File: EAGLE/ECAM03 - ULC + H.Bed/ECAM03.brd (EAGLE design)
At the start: 160 x 60 mm, 45 parts, among them J1 MODULAR TOOL, J2 FAN1, J3 FAN2, J4 FAN3, J5 B4B-PH-SM4, J6 SSR, J7 RINGLIGHT, J8 FTDI, J9 SPI, Q2 16MHz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

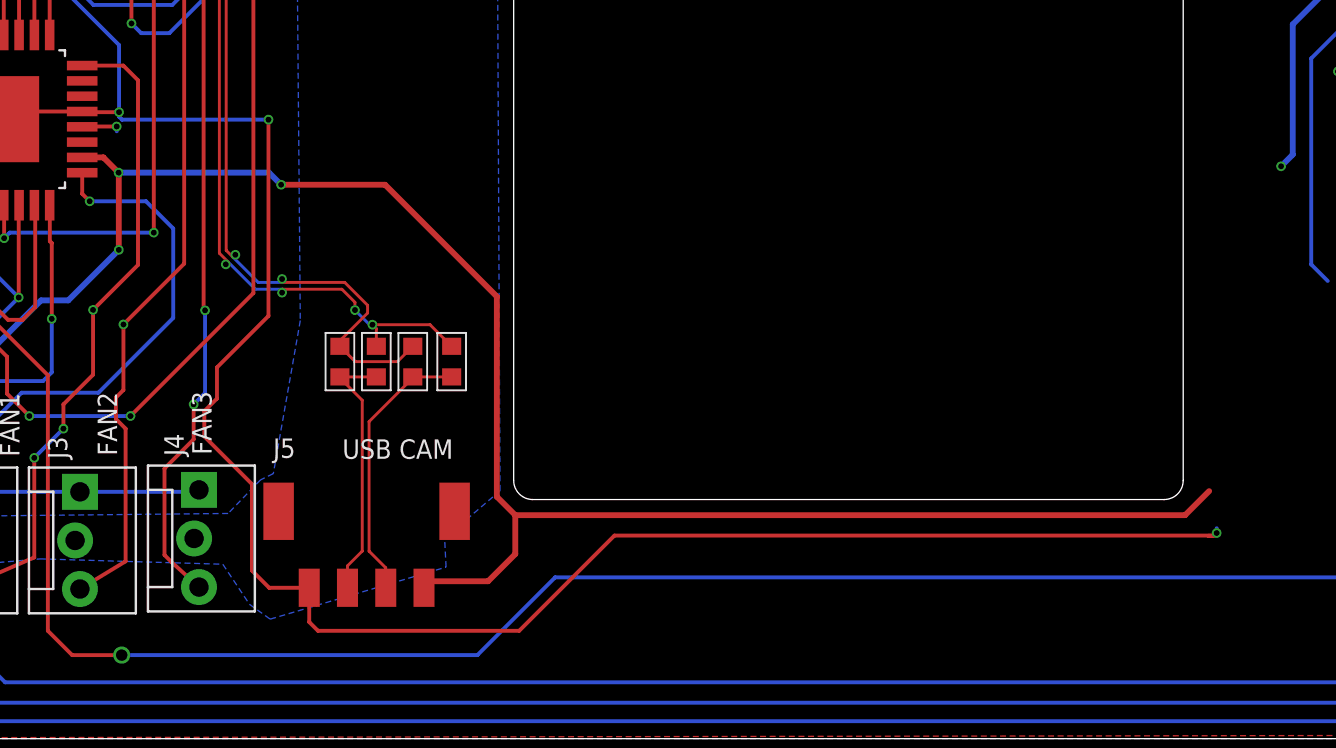
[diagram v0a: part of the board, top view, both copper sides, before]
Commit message: Fixed BOM, began adding DFM changes
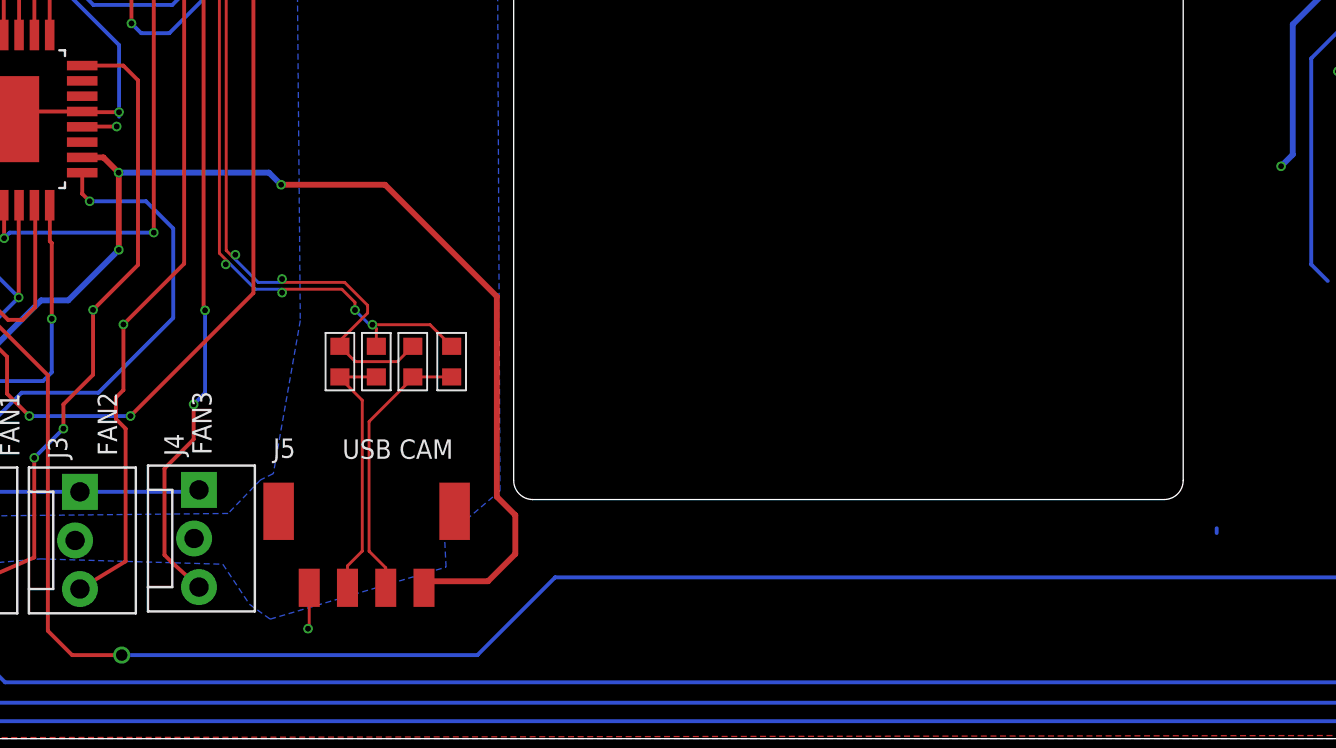
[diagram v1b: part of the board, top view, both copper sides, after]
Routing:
- net GND: track 327.0 -> 239.7 mm, vias 24 -> 23
- net +5V: track 241.3 -> 204.5 mm
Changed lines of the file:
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@@
 <?xml version="1.0" encoding="utf-8"?>
 <!DOCTYPE eagle SYSTEM "eagle.dtd">
-<eagle version="7.3.0">
+<eagle version="7.4.0">
 <drawing>
 <settings>
@@
 <grid distance="0.25" unitdist="mm" unit="mm" style="lines" multiple="1" display="yes" altdistance="0.001" altunitdist="inch" altunit="inch"/>
 <layers>
-<layer number="1" name="Top" color="4" fill="1" visible="no" active="yes"/>
-<layer number="2" name="Route2" color="1" fill="3" visible="no" active="yes"/>
+<layer number="1" name="Top" color="4" fill="1" visible="yes" active="yes"/>
+<layer number="2" name="Route2" color="1" fill="3" visible="yes" active="yes"/>
 <layer number="3" name="Route3" color="4" fill="3" visible="no" active="no"/>
 <layer number="4" name="Route4" color="1" fill="4" visible="no" active="no"/>
@@
 <layer number="13" name="Route13" color="4" fill="5" visible="no" active="no"/>
 <layer number="14" name="Route14" color="1" fill="6" visible="no" active="no"/>
-<layer number="15" name="Route15" color="4" fill="6" visible="no" active="yes"/>
-<layer number="16" name="Bottom" color="1" fill="1" visible="no" active="yes"/>
+<layer number="15" name="Route15" color="4" fill="6" visible="yes" active="yes"/>
+<layer number="16" name="Bottom" color="1" fill="1" visible="yes" active="yes"/>
 <layer number="17" name="Pads" color="2" fill="1" visible="yes" active="yes"/>
 <layer number="18" name="Vias" color="2" fill="1" visible="yes" active="yes"/>
-<layer number="19" name="Unrouted" color="6" fill="1" visible="no" active="yes"/>
+<layer number="19" name="Unrouted" color="6" fill="1" visible="yes" active="yes"/>
 <layer number="20" name="Dimension" color="15" fill="1" visible="yes" active="yes"/>
 <layer number="21" name="tPlace" color="7" fill="1" visible="yes" active="yes"/>
-<layer number="22" name="bPlace" color="7" fill="1" visible="no" active="yes"/>
-<layer number="23" name="tOrigins" color="15" fill="1" visible="no" active="yes"/>
-<layer number="24" name="bOrigins" color="15" fill="1" visible="no" active="yes"/>
+<layer number="22" name="bPlace" color="7" fill="1" visible="yes" active="yes"/>
+<layer number="23" name="tOrigins" color="15" fill="1" visible="yes" active="yes"/>
+<layer number="24" name="bOrigins" color="15" fill="1" visible="yes" active="yes"/>
 <layer number="25" name="tNames" color="7" fill="1" visible="yes" active="yes"/>
-<layer number="26" name="bNames" color="7" fill="1" visible="no" active="yes"/>
+<layer number="26" name="bNames" color="7" fill="1" visible="yes" active="yes"/>
 <layer number="27" name="tValues" color="7" fill="1" visible="no" active="yes"/>
 <layer number="28" name="bValues" color="7" fill="1" visible="no" active="yes"/>
-<layer number="29" name="tStop" color="7" fill="3" visible="no" active="yes"/>
-<layer number="30" name="bStop" color="7" fill="6" visible="no" active="yes"/>
+<layer number="29" name="tStop" color="7" fill="3" visible="yes" active="yes"/>
+<layer number="30" name="bStop" color="7" fill="6" visible="yes" active="yes"/>
 <layer number="31" name="tCream" color="7" fill="4" visible="yes" active="yes"/>
-<layer number="32" name="bCream" color="7" fill="5" visible="no" active="yes"/>
+<layer number="32" name="bCream" color="7" fill="5" visible="yes" active="yes"/>
 <layer number="33" name="tFinish" color="6" fill="3" visible="no" active="yes"/>
 <layer number="34" name="bFinish" color="6" fill="6" visible="no" active="yes"/>
@@
 <wire x1="25.4" y1="31.9532" x2="28.2702" y2="31.9532" width="0.2032" layer="16"/>
 <wire x1="28.2702" y1="31.9532" x2="28.321" y2="32.004" width="0.2032" layer="16"/>
-<via x="49.6824" y="32.3596" extent="1-16" drill="0.3048"/>
-<wire x1="49.6824" y1="22.098" x2="49.6824" y2="32.3596" width="0.2032" layer="1"/>
-<wire x1="49.6824" y1="32.3596" x2="42.0243" y2="32.3596" width="0.2032" layer="16"/>
-<wire x1="42.0243" y1="32.3596" x2="41.8719" y2="32.512" width="0.2032" layer="16"/>
-<wire x1="48.8188" y1="13.3096" x2="46.3296" y2="15.7988" width="0.2032" layer="1"/>
-<wire x1="46.3296" y1="15.7988" x2="46.3296" y2="17.1196" width="0.2032" layer="1"/>
-<wire x1="46.3296" y1="17.1196" x2="46.99" y2="17.78" width="0.2032" layer="1"/>
-<wire x1="46.99" y1="17.78" x2="46.99" y2="19.4056" width="0.2032" layer="1"/>
 <wire x1="40.2717" y1="51.0286" x2="40.2717" y2="49.3903" width="0.2032" layer="16"/>
 <wire x1="40.2717" y1="49.3903" x2="43.18" y2="46.482" width="0.2032" layer="16"/>
@@
 <wire x1="23.368" y1="27.1272" x2="23.8252" y2="26.67" width="0.2032" layer="16"/>
 <wire x1="23.8252" y1="26.67" x2="24.1808" y2="26.67" width="0.2032" layer="16"/>
-<wire x1="51.8132" y1="7.8867" x2="49.7205" y2="7.8867" width="0.2032" layer="1"/>
-<wire x1="49.7205" y1="7.8867" x2="48.8188" y2="8.7884" width="0.2032" layer="1"/>
-<wire x1="48.8188" y1="8.7884" x2="48.8188" y2="13.3096" width="0.2032" layer="1"/>
-<wire x1="51.8132" y1="7.8867" x2="51.8132" y2="6.0988" width="0.2032" layer="1"/>
-<wire x1="51.8132" y1="6.0988" x2="52.2732" y2="5.6388" width="0.2032" layer="1"/>
-<wire x1="52.2732" y1="5.6388" x2="62.7888" y2="5.6388" width="0.2032" layer="1"/>
-<wire x1="62.7888" y1="5.6388" x2="67.7672" y2="10.6172" width="0.2032" layer="1"/>
-<wire x1="67.7672" y1="10.6172" x2="99.1172" y2="10.6172" width="0.2032" layer="1"/>
 <contactref element="J7" pad="3"/>
-<wire x1="46.99" y1="19.4056" x2="49.6824" y2="22.098" width="0.2032" layer="1"/>
 <wire x1="39.9457" y1="32.785" x2="35.8457" y2="32.785" width="0.2032" layer="1"/>
 <wire x1="35.8457" y1="32.785" x2="35.4457" y2="32.385" width="0.2032" layer="1"/>
@@
 <wire x1="114.7318" y1="27.7434" x2="114.7064" y2="27.718" width="0.254" layer="1"/>
 <wire x1="115.6818" y1="25.3934" x2="115.6716" y2="25.4036" width="0.254" layer="1"/>
-<polygon width="0.254" layer="16" rank="3">
+<polygon width="0.254" layer="16" thermals="no" rank="3">
 <vertex x="0" y="60"/>
 <vertex x="160" y="60"/>
@@
 <vertex x="0" y="0"/>
 </polygon>
-<wire x1="98.806" y1="10.6045" x2="99.1045" y2="10.6045" width="0.2032" layer="1"/>
-<wire x1="99.1045" y1="10.6045" x2="99.25" y2="10.75" width="0.2032" layer="1"/>
-<via x="99.25" y="10.75" extent="1-16" drill="0.3048"/>
 <wire x1="99.25" y1="10.75" x2="99.25" y2="11" width="0.2032" layer="16"/>
-<wire x1="99.1172" y1="10.6172" x2="99.25" y2="10.75" width="0.2032" layer="1"/>
 <wire x1="114.7064" y1="27.718" x2="114.9564" y2="28.9564" width="0.2032" layer="1"/>
 <wire x1="114.9564" y1="28.9564" x2="115" y2="29" width="0.2032" layer="1"/>
@@
 <wire x1="39.9607" y1="32" x2="41.75" y2="32" width="0.2032" layer="1"/>
 <via x="41.75" y="32" extent="1-16" drill="0.3048"/>
-<wire x1="41.75" y1="32" x2="41.75" y2="31.75" width="0.2032" layer="16"/>
+<via x="51.75" y="5.75" extent="1-16" drill="0.3048"/>
+<wire x1="51.8132" y1="7.8867" x2="51.8132" y2="5.8132" width="0.1524" layer="1"/>
+<wire x1="51.8132" y1="5.8132" x2="51.75" y2="5.75" width="0.1524" layer="1"/>
 </signal>
 <signal name="+5V">
@@
 <contactref element="J5" pad="4"/>
 <wire x1="113.7818" y1="27.7434" x2="113.7818" y2="27.8994" width="0.3048" layer="1"/>
-<wire x1="97.5995" y1="11.684" x2="62.5856" y2="11.684" width="0.3048" layer="1"/>
 <contactref element="VR1" pad="1"/>
 <contactref element="VR1" pad="3"/>
@@
 <wire x1="41.0525" y1="30.385" x2="41.8465" y2="29.591" width="0.3048" layer="1"/>
 <via x="41.8465" y="29.591" extent="1-16" drill="0.3048"/>
-<wire x1="98.8568" y1="12.9413" x2="97.5995" y2="11.684" width="0.3048" layer="1"/>
 <wire x1="10.0584" y1="31.496" x2="10.0584" y2="39.7764" width="0.3048" layer="16"/>
 <wire x1="10.0584" y1="39.7764" x2="10.668" y2="40.386" width="0.3048" layer="16"/>
@@
 <wire x1="117.348" y1="43.3324" x2="117.348" y2="44.0816" width="0.3048" layer="1"/>
 <wire x1="117.348" y1="44.0816" x2="119.2404" y2="45.974" width="0.3048" layer="1"/>
-<polygon width="0.2032" layer="1" rank="3">
+<polygon width="0.2032" layer="1" thermals="no" rank="3">
 <vertex x="0" y="60"/>
 <vertex x="160" y="60"/>

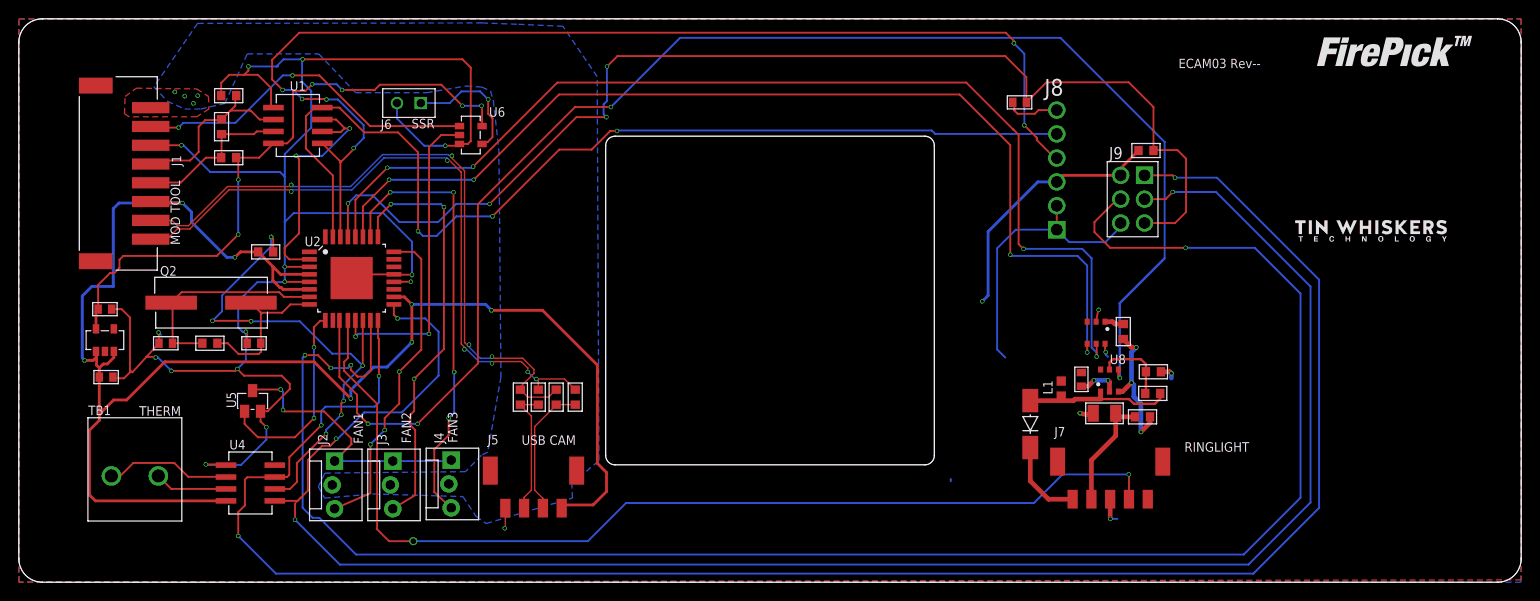
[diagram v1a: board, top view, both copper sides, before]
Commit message: Added decoupling caps to EFD01, ECAM02, rearranged parts for better fit, increased power trace width, updated BOM and database.
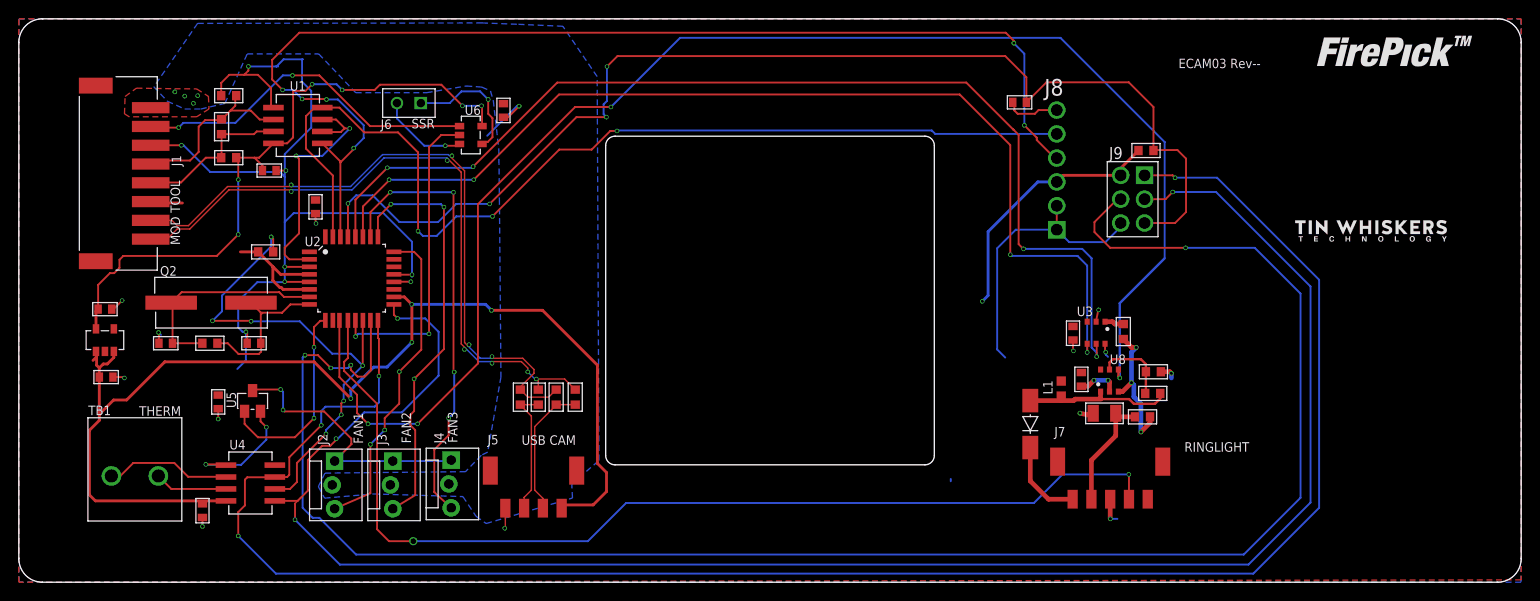
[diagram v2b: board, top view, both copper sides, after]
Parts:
- added C1, C10, C11, C2, C3, C9: 0.1uF, TinWhiskers:C0603
- U2: device TinWhiskers:32-TQFN -> TinWhiskers:32-TQF(ATMEGA)
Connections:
- net +3V3: now also C2.2
- net +5V: now also C1.2, C10.2, C11.2, C3.2, C9.2
- net GND: now also C1.1, C10.1, C11.1, C2.1, C3.1, C9.1; no longer U2.PAD
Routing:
- net GND: track 239.7 -> 186.5 mm, vias 23 -> 27
- net +5V: track 204.5 -> 167.6 mm, vias 8 -> 5
- net +3V3: track 66.6 -> 68.3 mm

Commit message: Made REV 2 modifications, including increasing width of power traces, adding vias to power traces, and addition of LEDs to all modular tools. Catch diodes added to ESOL01 board to prevent coils from creating problems "upstream"
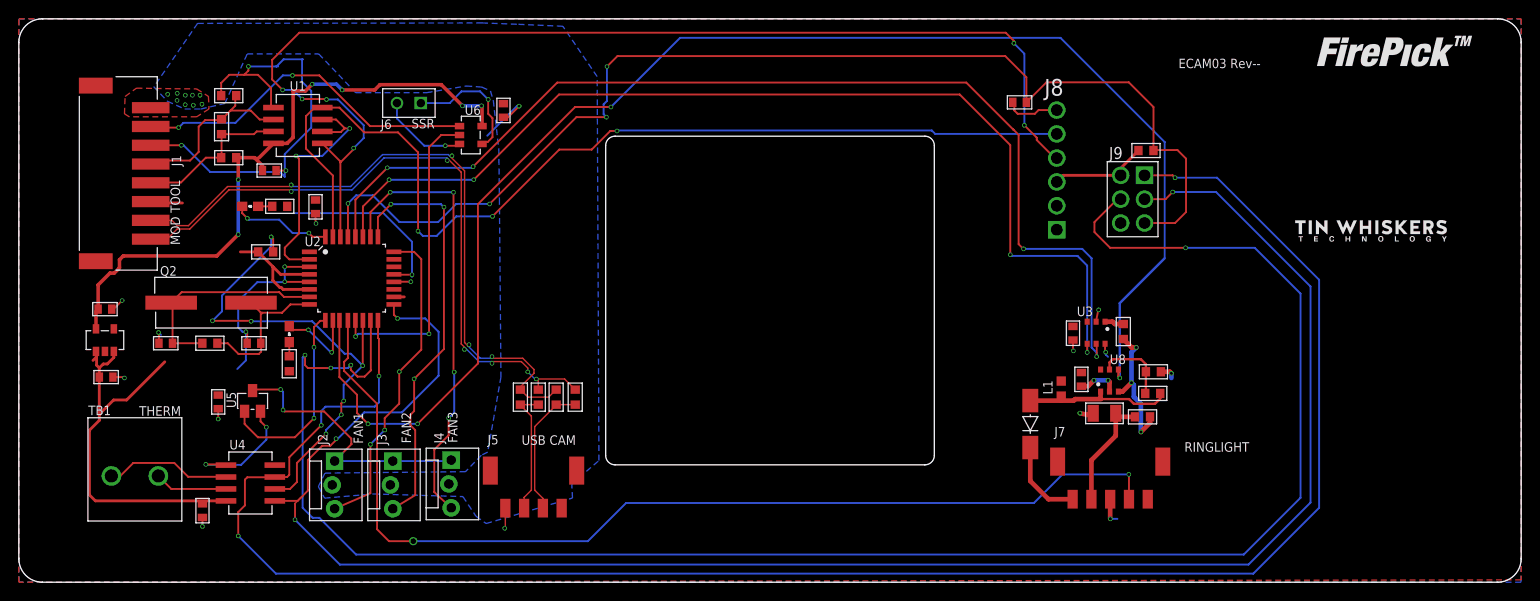
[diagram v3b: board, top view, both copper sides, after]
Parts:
- added LED1, LED2: RED, TinWhiskers:LED0603
- added R17, R5: 1K, TinWhiskers:R0603
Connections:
- new net N$1: LED2.A, R17.1
- new net N$2: LED1.A, R5.1
- new net N$3: LED1.C, U2.32
- new net N$4: LED2.C, U2.10
- net +5V: now also R17.2, R5.2
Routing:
- net +5V: track 167.6 -> 72.5 mm, vias 5 -> 0
- net GND: track 186.5 -> 145.1 mm
- net N$3: track 0.00 -> 10.6 mm, vias 0 -> 2
- net N$4: track 0.00 -> 9.12 mm, vias 0 -> 2
- net N$2: track 0.00 -> 1.50 mm
- net N$1: track 0.00 -> 1.50 mm
- net MOSI: track 192.6 -> 193.2 mm
